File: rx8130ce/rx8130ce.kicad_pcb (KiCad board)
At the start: 2 copper layers, 25.4 x 17.8 mm, 12 parts, among them J3 Conn_01x05, J4 Conn_01x05, U1 RX8130CE

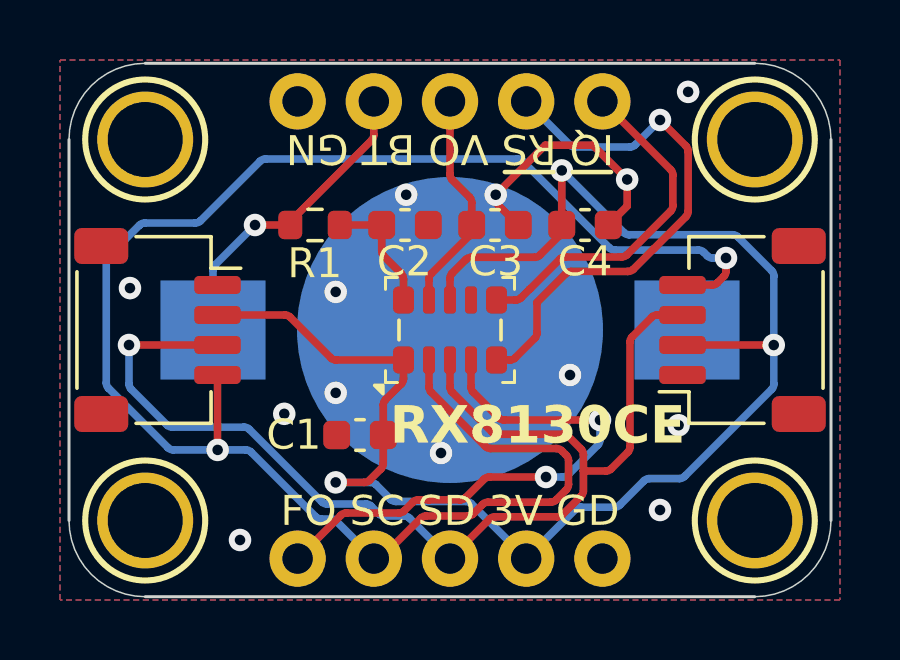
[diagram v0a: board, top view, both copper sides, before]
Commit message: bump to KiCAD 10
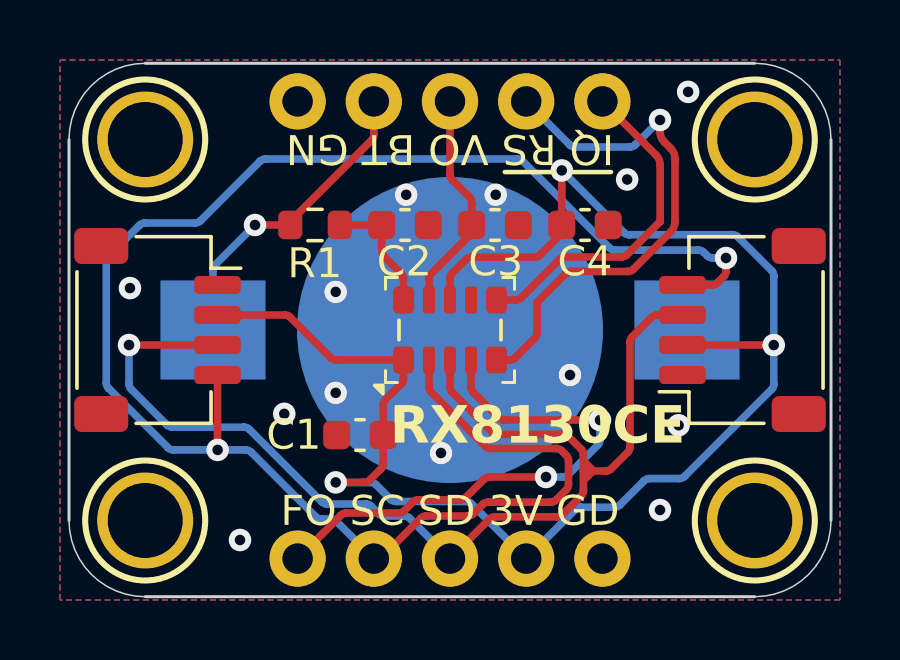
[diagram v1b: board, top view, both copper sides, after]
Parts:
- REF**: moved to B.Cu
- turned REF** to 180 degrees
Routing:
- net GND: track 8.64 -> 0.26 mm
